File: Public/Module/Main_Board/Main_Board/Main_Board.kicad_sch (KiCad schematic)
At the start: 13 parts, among them J1 Conn_02x28_Odd_Even, J10 Conn_01x08, J2 Conn_02x28_Odd_Even, J3 Conn_02x28_Odd_Even, J4 Conn_02x28_Odd_Even, J5 Conn_01x04, J6 Conn_01x05, J7 Conn_01x05, J8 Conn_01x04, J9 Conn_01x04

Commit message: 主板原理图
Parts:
- removed J1: Conn_02x28_Odd_Even, NEUDC:MCU_right, symbol Connector_Generic:Conn_02x28_Odd_Even
- removed J10: Conn_01x08, symbol Connector_Generic:Conn_01x08
- removed J2: Conn_02x28_Odd_Even, NEUDC:MCU_left, symbol Connector_Generic:Conn_02x28_Odd_Even
- removed J5, J8, J9: Conn_01x04, symbol Connector_Generic:Conn_01x04
- removed U1: ~, symbol NEUDC:qimin
- added C1, C2: 10uF, symbol Device:C
- added J1, J12: Conn_01x02, symbol Connector_Generic:Conn_01x02
- added J10, J11: Conn_01x24, symbol Connector_Generic:Conn_01x24
- added J13, J14, J5: Conn_01x03, symbol Connector_Generic:Conn_01x03
- added U1: LM1117MP-3.3, Package_TO_SOT_SMD:SOT-223-3_TabPin2, symbol Regulator_Linear:LM1117MP-3.3
- added U2: ~, NEUDC:qimin, symbol NEUDC:qimin
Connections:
- net PG0 is gone; now on net SPI1_CS: J3.17 (Pin_17)
- net PG1 is gone; now on net SPI1_CS: J3.16 (Pin_16)
- net 3V3: now also C2.1, J1.2 (Pin_2), U1.2 (VO); no longer J6.5 (Pin_5), J7.5 (Pin_5)
- net GNDREF: now also C1.2, C2.2, J1.1 (Pin_1), J12.1 (Pin_1), J13.1 (Pin_1), J14.1 (Pin_1), J5.1 (Pin_1), U1.1 (GND), U2.58 (Pin_58)
- net I2C1_SCL: now also J13.3 (Pin_3), U2.52 (Pin_52)
- net I2C1_SDA: now also J13.2 (Pin_2), U2.51 (Pin_51)
- net PA10: now also U2.23 (Pin_23)
- net PA11: now also U2.26 (Pin_26)
- net PA12: now also U2.25 (Pin_25)
- net PA13: now also U2.28 (Pin_28)
- net PA14: now also U2.27 (Pin_27)
- net PA15: now also J10.5 (Pin_5), U2.30 (Pin_30)
- net PA4: now also J10.1 (Pin_1), U2.87 (Pin_87)
- net PA5: now also U2.86 (Pin_86)
- net PA6: now also J10.2 (Pin_2), U2.85 (Pin_85)
- net PA7: now also J10.3 (Pin_3), U2.84 (Pin_84)
- net PA8: now also J10.4 (Pin_4), U2.21 (Pin_21)
- net PA9: now also U2.24 (Pin_24)
- net PB0: now also U2.81 (Pin_81)
- net PB1: now also U2.80 (Pin_80)
- net PB10: now also U2.62 (Pin_62)
- net PB11: now also U2.61 (Pin_61)
- net PB12: now also J10.8 (Pin_8), U2.60 (Pin_60)
- net PB2: now also U2.79 (Pin_79)
- net PB8: now also J10.6 (Pin_6), U2.54 (Pin_54)
- net PB9: now also J10.7 (Pin_7), U2.53 (Pin_53)
- net PC10: now also J10.17 (Pin_17), U2.29 (Pin_29)
- net PC11: now also J10.18 (Pin_18), U2.32 (Pin_32)
- net PC12: now also J10.19 (Pin_19), U2.31 (Pin_31)
- net PC13: now also J10.20 (Pin_20), U2.107 (Pin_107)
- net PC2: now also J10.9 (Pin_9), U2.93 (Pin_93)
- net PC3: now also J10.10 (Pin_10), U2.92 (Pin_92)
- net PC4: now also J10.11 (Pin_11), U2.83 (Pin_83)
- net PC5: now also J10.12 (Pin_12), U2.82 (Pin_82)
- net PC6: now also J10.13 (Pin_13), U2.17 (Pin_17)
- net PC7: now also J10.14 (Pin_14), U2.20 (Pin_20)
- net PC8: now also J10.15 (Pin_15), U2.19 (Pin_19)
- net PC9: now also J10.16 (Pin_16), U2.22 (Pin_22)
- net PD0: now also U2.34 (Pin_34)
- net PD1: now also U2.33 (Pin_33)
- net PD10: now also U2.6 (Pin_6)
- net PD11: now also U2.5 (Pin_5)
- net PD12: now also U2.8 (Pin_8)
- net PD13: now also U2.7 (Pin_7)
- net PD14: now also U2.10 (Pin_10)
- net PD15: now also U2.9 (Pin_9)
- net PD2: now also U2.36 (Pin_36)
- net PD3: now also U2.35 (Pin_35)
- net PD4: now also U2.38 (Pin_38)
- net PD5: now also U2.37 (Pin_37)
- net PD6: now also U2.40 (Pin_40)
- net PD7: now also U2.39 (Pin_39)
- net PD8: now also U2.4 (Pin_4)
- net PD9: now also U2.3 (Pin_3)
- net PE0: now also U2.56 (Pin_56)
- net PE1: now also U2.55 (Pin_55)
- net PE10: now also U2.68 (Pin_68)
- net PE11: now also U2.67 (Pin_67)
- net PE12: now also U2.66 (Pin_66)
- net PE13: now also U2.65 (Pin_65)
- net PE14: now also U2.64 (Pin_64)
- net PE15: now also U2.63 (Pin_63)
- net PE2: now also J10.21 (Pin_21), U2.112 (Pin_112)
- net PE3: now also J10.22 (Pin_22), U2.111 (Pin_111)
- net PE4: now also J10.23 (Pin_23), U2.110 (Pin_110)
- net PE5: now also J10.24 (Pin_24), U2.109 (Pin_109)
- net PE6: now also J11.1 (Pin_1), U2.108 (Pin_108)
- net PE7: now also U2.71 (Pin_71)
- net PE8: now also U2.70 (Pin_70)
- net PE9: now also U2.69 (Pin_69)
- net PF0: now also J11.2 (Pin_2), U2.106 (Pin_106)
- net PF1: now also J11.3 (Pin_3), U2.105 (Pin_105)
- net PF10: now also J11.12 (Pin_12), U2.96 (Pin_96)
- net PF11: now also J11.13 (Pin_13), U2.78 (Pin_78)
- net PF12: now also J11.14 (Pin_14), U2.77 (Pin_77)
- net PF13: now also J11.15 (Pin_15), U2.76 (Pin_76)
- net PF14: now also J11.16 (Pin_16), U2.75 (Pin_75)
- net PF15: now also J11.17 (Pin_17), U2.74 (Pin_74)
- net PF2: now also J11.4 (Pin_4), U2.104 (Pin_104)
- net PF3: now also J11.5 (Pin_5), U2.103 (Pin_103)
- net PF4: now also J11.6 (Pin_6), U2.102 (Pin_102)
- net PF5: now also J11.7 (Pin_7), U2.101 (Pin_101)
- net PF6: now also J11.8 (Pin_8), U2.100 (Pin_100)
- net PF7: now also J11.9 (Pin_9), U2.99 (Pin_99)
- net PF8: now also J11.10 (Pin_10), U2.98 (Pin_98)
- net PF9: now also J11.11 (Pin_11), U2.97 (Pin_97)
- net PG10: now also U2.41 (Pin_41)
- net PG11: now also U2.44 (Pin_44)
- net PG12: now also U2.43 (Pin_43)
- net PG13: now also U2.46 (Pin_46)
- net PG14: now also U2.45 (Pin_45)
- net PG15: now also U2.48 (Pin_48)
- net PG2: now also J11.20 (Pin_20), U2.12 (Pin_12)
- net PG3: now also J11.21 (Pin_21), U2.11 (Pin_11)
- net PG4: now also J11.22 (Pin_22), U2.14 (Pin_14)
- net PG5: now also J11.23 (Pin_23), U2.13 (Pin_13)
- net PG6: now also J11.24 (Pin_24), U2.16 (Pin_16)
- net PG7: now also U2.15 (Pin_15)
- net PG8: now also U2.18 (Pin_18)
- net PG9: now also U2.42 (Pin_42)
- net SPI1_CLK: now also U2.47 (Pin_47)
- net SPI1_MISO: now also U2.50 (Pin_50)
- net SPI1_MOSI: now also U2.49 (Pin_49)
- net SPI2_CLK: now also U2.59 (Pin_59)
- net SPI2_MISO: now also U2.1 (Pin_1)
- net SPI2_MOSI: now also U2.2 (Pin_2)
- net USART2_RX: now also J14.2 (Pin_2), U2.88 (Pin_88)
- net USART2_TX: now also J14.3 (Pin_3), U2.89 (Pin_89)
- net USART4_RX: now also J5.2 (Pin_2), U2.90 (Pin_90)
- net USART4_TX: now also J5.3 (Pin_3), U2.91 (Pin_91)
- net VCC5: now also C1.1, J12.2 (Pin_2), U1.3 (VI), U2.57 (Pin_57)
- net PC0 renamed SPI1_CS
- net SPI1_CS: now also J6.5 (Pin_5), J11.18 (Pin_18), J11.19 (Pin_19), U2.72 (Pin_72), U2.73 (Pin_73), U2.95 (Pin_95)
- net PC1 renamed SPI2_CS
- net SPI2_CS: now also J7.5 (Pin_5), U2.94 (Pin_94)

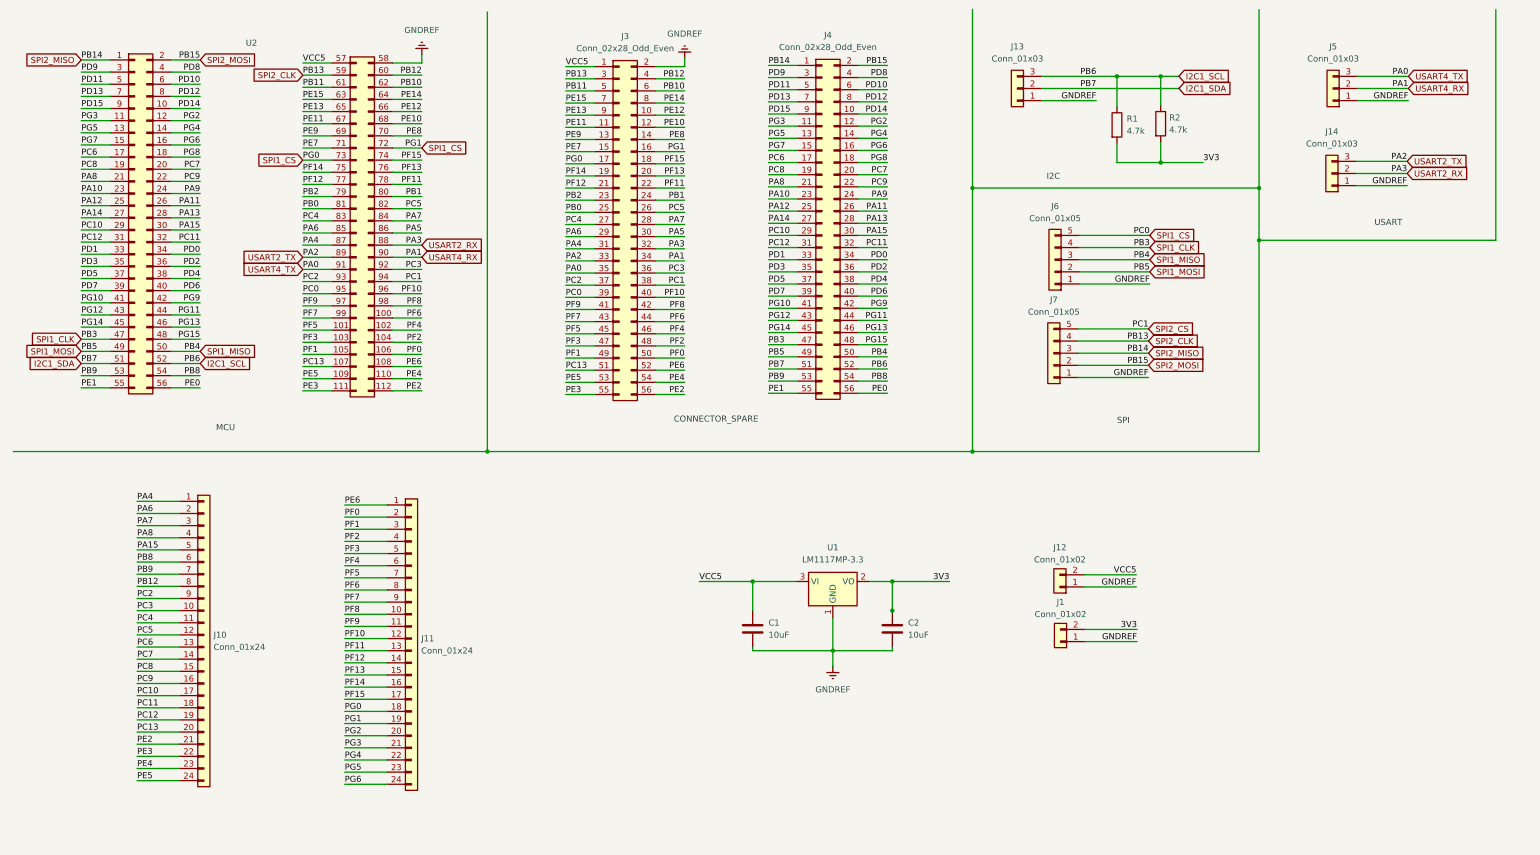
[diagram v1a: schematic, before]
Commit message: 主板修改（电容断连 分割线修改）
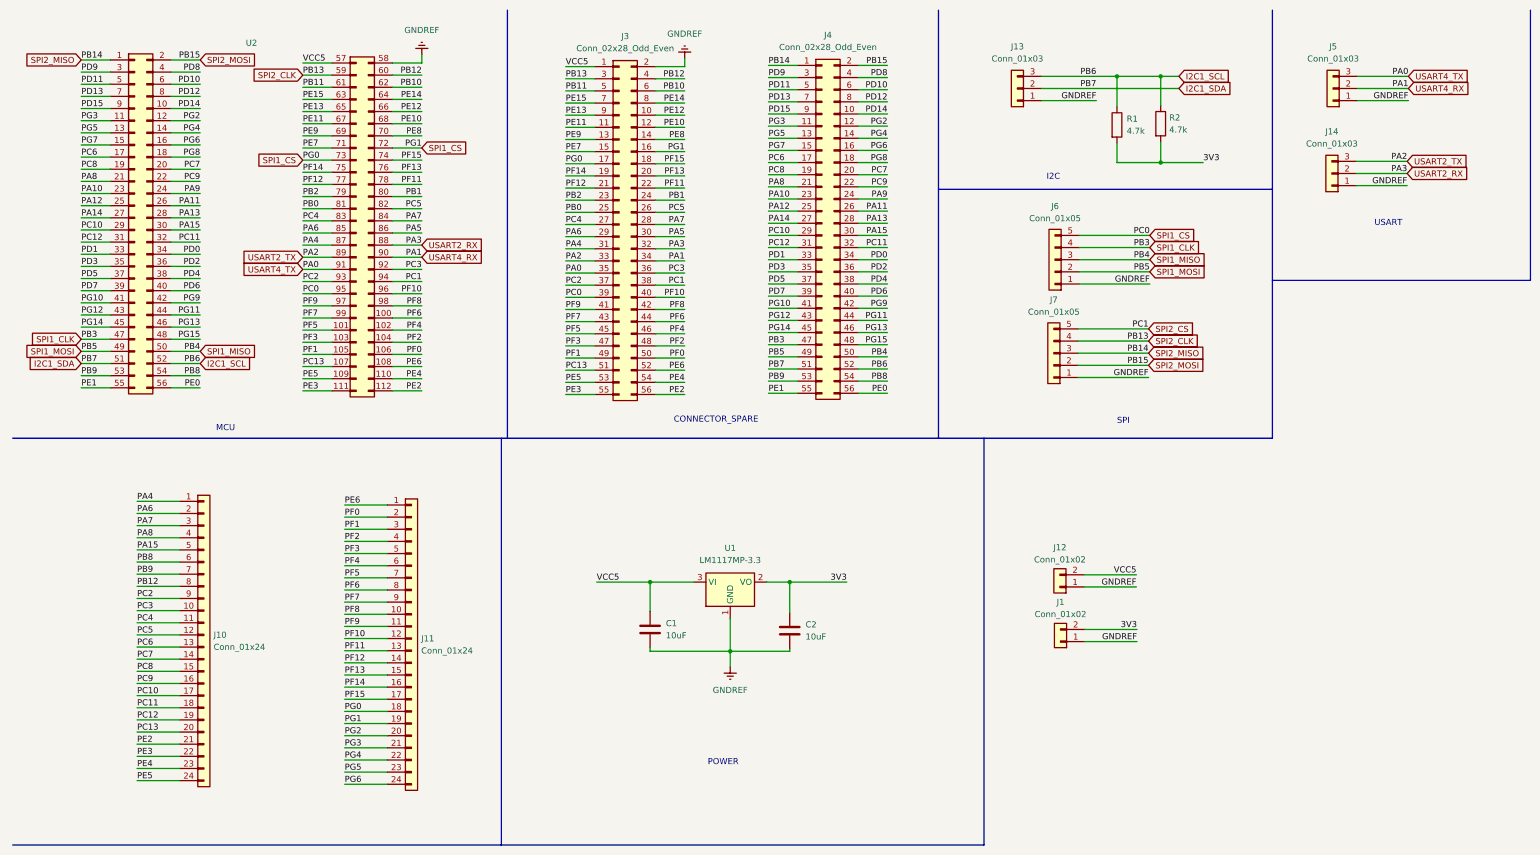
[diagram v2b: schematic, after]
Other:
- note added: "POWER"
- moved on the sheet: C1, C2, U1

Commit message: 主板PCB绘制
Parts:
- C1, C2: footprint (none) -> Capacitor_SMD:C_1206_3216Metric
- J1, J12: footprint (none) -> NEUDC:Con_1_2
- J10, J11: footprint (none) -> NEUDC:Con_1_24
- J13, J14, J5: footprint (none) -> NEUDC:Con_1_3
- J6, J7: footprint (none) -> NEUDC:Con_1_5
- R1, R2: footprint (none) -> Resistor_SMD:R_1206_3216Metric
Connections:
- net I2C1_SCL: no longer R2.1
- net I2C1_SDA: now also R2.1
- net SPI1_CS: no longer J11.18 (Pin_18), J11.19 (Pin_19), J3.16 (Pin_16), J3.17 (Pin_17), U2.72 (Pin_72), U2.73 (Pin_73)
- new net PG0: J11.18 (Pin_18), J3.17 (Pin_17), U2.73 (Pin_73)
- new net PG1: J11.19 (Pin_19), J3.16 (Pin_16), U2.72 (Pin_72)
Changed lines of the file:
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@@
   (junction (at 252.222 43.942) (diameter 0) (color 0 0 0 0)
   )
-  (junction (at 252.222 25.908) (diameter 0) (color 0 0 0 0)
-  )
   (junction (at 162.179 146.177) (diameter 0) (color 0 0 0 0)
   )
+  (junction (at 252.222 28.448) (diameter 0) (color 0 0 0 0)
+  )
   (wire (pts (xy 236.22 132.715) (xy 247.142 132.715))
     (stroke (width 0) (type default))
@@
     (stroke (width 0) (type default))
   )
-  (wire (pts (xy 243.078 25.908) (xy 252.222 25.908))
+  (wire (pts (xy 243.078 25.908) (xy 256.032 25.908))
     (stroke (width 0) (type default))
   )
@@
     (stroke (width 0) (type default))
   )
+  (wire (pts (xy 252.222 28.448) (xy 252.222 32.004))
+    (stroke (width 0) (type default))
+  )
   (wire (pts (xy 170.18 84.582) (xy 176.276 84.582))
     (stroke (width 0) (type default))
@@
     (stroke (width 0) (type default))
   )
+  (wire (pts (xy 252.222 28.448) (xy 256.032 28.448))
+    (stroke (width 0) (type default))
+  )
   (wire (pts (xy 81.534 168.91) (xy 90.424 168.91))
     (stroke (width 0) (type default))
@@
     (stroke (width 0) (type default))
   )
-  (wire (pts (xy 252.222 25.908) (xy 256.032 25.908))
-    (stroke (width 0) (type default))
-  )
   (wire (pts (xy 146.558 61.976) (xy 152.654 61.976))
     (stroke (width 0) (type default))
@@
     (stroke (width 0) (type default))
   )
-  (wire (pts (xy 252.222 25.908) (xy 252.222 32.004))
-    (stroke (width 0) (type default))
-  )
   (wire (pts (xy 127.762 79.756) (xy 133.858 79.756))
     (stroke (width 0) (type default))
@@
     (stroke (width 0) (type default))
   )
-  (wire (pts (xy 227.33 28.448) (xy 256.032 28.448))
+  (wire (pts (xy 227.33 28.448) (xy 252.222 28.448))
     (stroke (width 0) (type default))
   )
@@
     )
   )
-  (global_label "SPI1_CS" (shape input) (at 72.771 43.434 180) (fields_autoplaced)
+  (global_label "SPI1_CS" (shape input) (at 72.771 71.374 180) (fields_autoplaced)
     (effects (font (size 1.27 1.27)) (justify right))
-    (property "Intersheetrefs" "${INTERSHEET_REFS}" (at 62.0449 43.434 0)
+    (property "Intersheetrefs" "${INTERSHEET_REFS}" (at 62.0449 71.374 0)
       (effects (font (size 1.27 1.27)) (justify right) hide)
     )
@@
     )
   )
-  (global_label "SPI1_CS" (shape input) (at 97.663 40.894 0) (fields_autoplaced)
+  (global_label "SPI2_CS" (shape input) (at 97.663 68.834 0) (fields_autoplaced)
     (effects (font (size 1.27 1.27)) (justify left))
-    (property "Intersheetrefs" "${INTERSHEET_REFS}" (at 108.3891 40.894 0)
+    (property "Intersheetrefs" "${INTERSHEET_REFS}" (at 108.3891 68.834 0)
       (effects (font (size 1.27 1.27)) (justify left) hide)
     )
@@
       (effects (font (size 1.27 1.27)))
     )
-    (property "Footprint" "" (at 229.87 83.82 0)
+    (property "Footprint" "NEUDC:Con_1_5" (at 229.87 83.82 0)
       (effects (font (size 1.27 1.27)) hide)
     )
@@
       (effects (font (size 1.27 1.27)) (justify left))
     )
-    (property "Footprint" "" (at 241.3 36.068 90)
+    (property "Footprint" "Resistor_SMD:R_1206_3216Metric" (at 241.3 36.068 90)
       (effects (font (size 1.27 1.27)) hide)
     )
@@
       (effects (font (size 1.27 1.27)) (justify left))
     )
-    (property "Footprint" "" (at 250.444 35.814 90)
+    (property "Footprint" "Resistor_SMD:R_1206_3216Metric" (at 250.444 35.814 90)
       (effects (font (size 1.27 1.27)) hide)
     )
@@
       (effects (font (size 1.27 1.27)))
     )
-    (property "Footprint" "" (at 231.267 144.145 0)
+    (property "Footprint" "NEUDC:Con_1_2" (at 231.267 144.145 0)
       (effects (font (size 1.27 1.27)) hide)
     )
@@
       (effects (font (size 1.27 1.27)))
     )
-    (property "Footprint" "" (at 230.124 64.262 0)
+    (property "Footprint" "NEUDC:Con_1_5" (at 230.124 64.262 0)
       (effects (font (size 1.27 1.27)) hide)
     )
@@
       (effects (font (size 1.27 1.27)))
     )
-    (property "Footprint" "" (at 288.29 28.448 0)
+    (property "Footprint" "NEUDC:Con_1_3" (at 288.29 28.448 0)
       (effects (font (size 1.27 1.27)) hide)
     )
@@
       (effects (font (size 1.27 1.27)))
     )
-    (property "Footprint" "" (at 222.25 28.448 0)
+    (property "Footprint" "NEUDC:Con_1_3" (at 222.25 28.448 0)
       (effects (font (size 1.27 1.27)) hide)
     )
@@
       (effects (font (size 1.27 1.27)) (justify left))
     )
-    (property "Footprint" "" (at 95.504 143.51 0)
+    (property "Footprint" "NEUDC:Con_1_24" (at 95.504 143.51 0)
       (effects (font (size 1.27 1.27)) hide)
     )
@@
       (effects (font (size 1.27 1.27)))
     )
-    (property "Footprint" "" (at 288.036 46.228 0)
+    (property "Footprint" "NEUDC:Con_1_3" (at 288.036 46.228 0)
       (effects (font (size 1.27 1.27)) hide)
     )
@@
       (effects (font (size 1.27 1.27)))
     )
-    (property "Footprint" "" (at 231.14 132.715 0)
+    (property "Footprint" "NEUDC:Con_1_2" (at 231.14 132.715 0)
       (effects (font (size 1.27 1.27)) hide)
     )
@@
       (effects (font (size 1.27 1.27)) (justify left))
     )
-    (property "Footprint" "" (at 52.07 142.748 0)
+    (property "Footprint" "NEUDC:Con_1_24" (at 52.07 142.748 0)
       (effects (font (size 1.27 1.27)) hide)
     )
@@
       (effects (font (size 1.27 1.27)) (justify left))
     )
-    (property "Footprint" "" (at 146.3802 145.415 0)
+    (property "Footprint" "Capacitor_SMD:C_1206_3216Metric" (at 146.3802 145.415 0)
       (effects (font (size 1.27 1.27)) hide)
     )
@@
       (effects (font (size 1.27 1.27)) (justify left))
     )
-    (property "Footprint" "" (at 175.5902 145.669 0)
-      (effects (font (size 1.27 1.27)) hide)
-    )
+    (property "Footprint" "Capacitor_SMD:C_1206_3216Metric" (at 175.5902 145.669 0)
+      (effects (font (size 1.27 1.27)) hide)
+    )
